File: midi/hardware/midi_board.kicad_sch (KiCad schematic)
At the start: 14 parts, among them J1 8bit_thing_bus_connector, J2 MIDI IN, J3 MIDI OUT, U1 TL16C2550PFB, U2 SLG46826G, U3 SLG46826G, U4 6N137, X1 SG-7050CCN

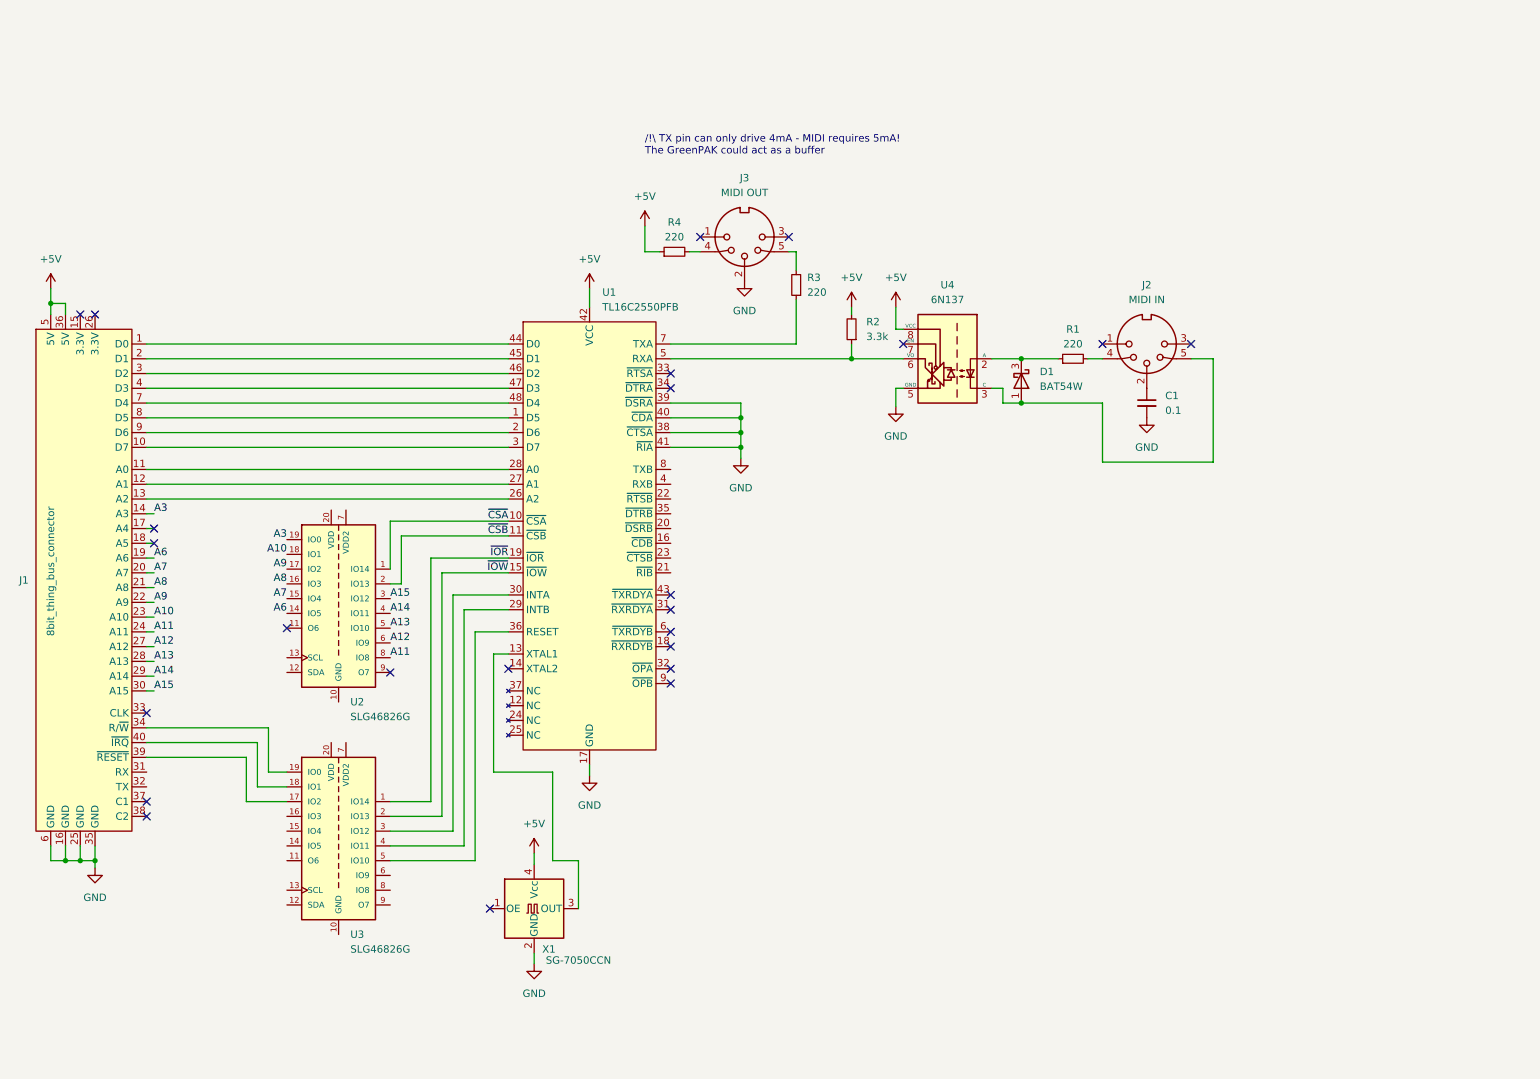
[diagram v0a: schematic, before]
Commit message: MIDI board v1 schematic & PCB
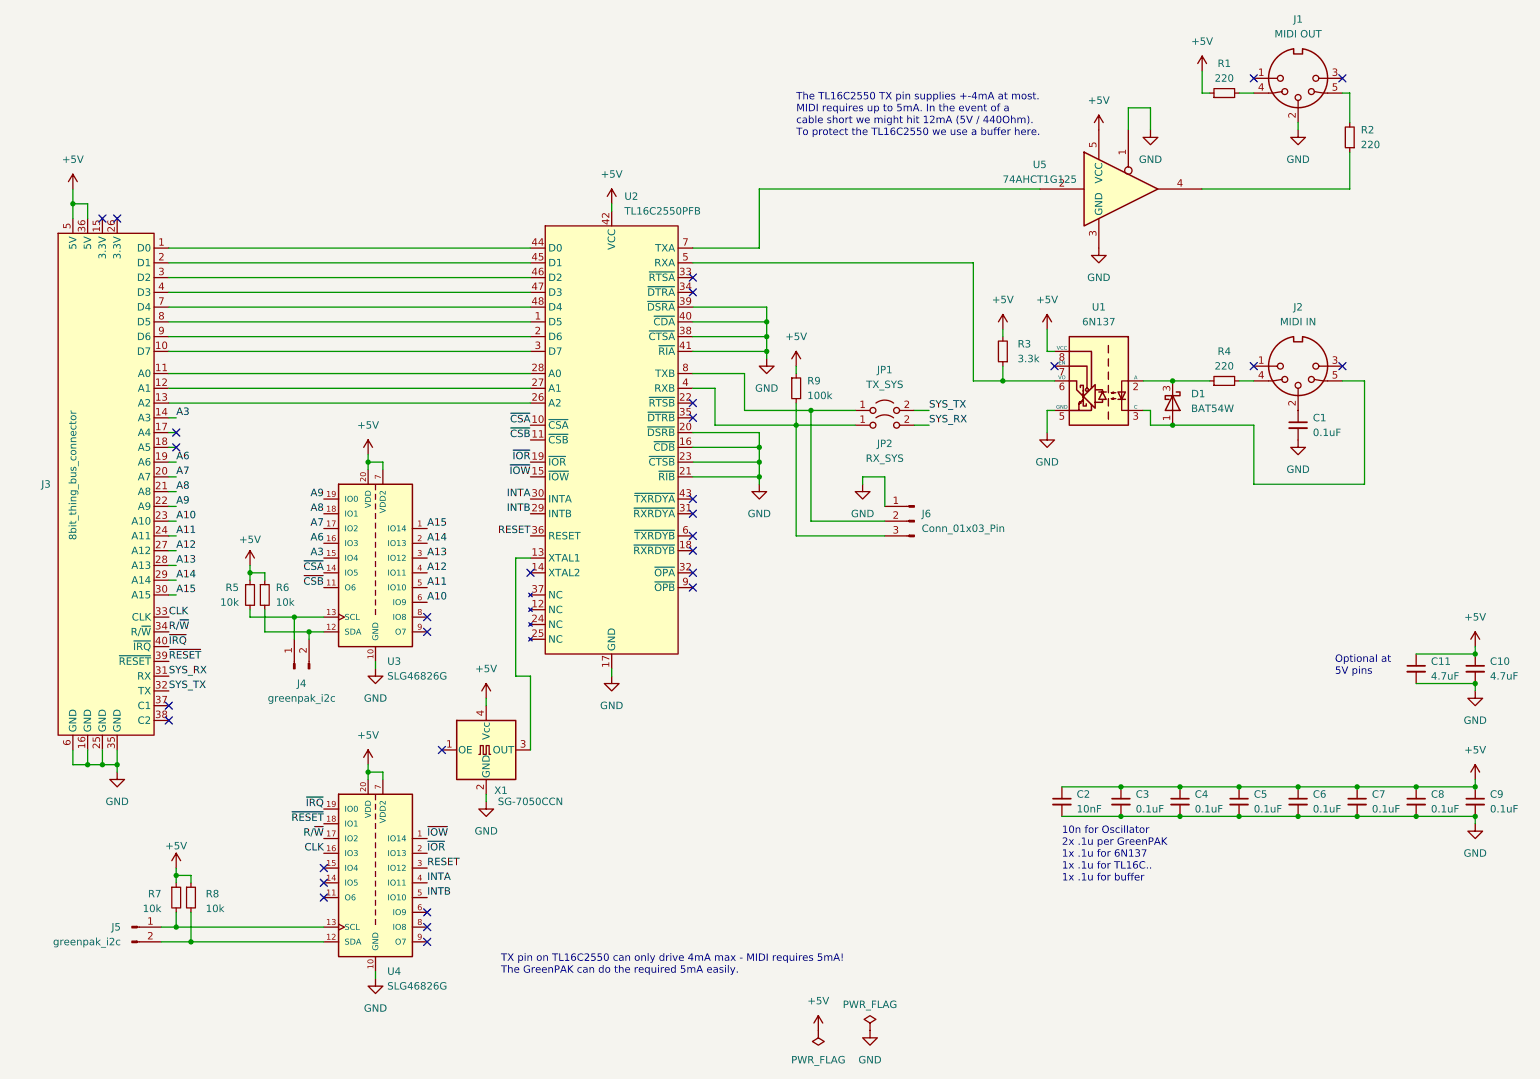
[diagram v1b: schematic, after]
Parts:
- removed J3: MIDI OUT, symbol Connector:DIN-5_180degree
- removed R3, R4: 220, symbol Device:R_Small
- added C10, C11: 4.7uF, Capacitor_SMD:C_0805_2012Metric_Pad1.18x1.45mm_HandSolder, symbol Device:C_Small
- added C2: 10nF, Capacitor_SMD:C_0805_2012Metric_Pad1.18x1.45mm_HandSolder, symbol Device:C_Small
- added C3, C4, C5, C6, C7, C8, C9: 0.1uF, Capacitor_SMD:C_0805_2012Metric_Pad1.18x1.45mm_HandSolder, symbol Device:C_Small
- added J1: MIDI OUT, own_footprints:Kycon-KCDX-5S-N, symbol Connector:DIN-5_180degree
- added J4, J5: greenpak_i2c, own_footprints:PinHeader_1x02_P2.54mm_Vertical_minimal, symbol Connector:Conn_01x02_Pin
- added J6: Conn_01x03_Pin, Connector_PinHeader_2.54mm:PinHeader_1x03_P2.54mm_Horizontal, symbol Connector:Conn_01x03_Pin
- added JP1: TX_SYS, own_footprints:PinHeader_1x02_P2.54mm_Vertical_minimal, symbol Jumper:Jumper_2_Open
- added JP2: RX_SYS, own_footprints:PinHeader_1x02_P2.54mm_Vertical_minimal, symbol Jumper:Jumper_2_Open
- added R1, R2: 220, Resistor_SMD:R_0805_2012Metric_Pad1.20x1.40mm_HandSolder, symbol Device:R_Small
- added R5, R6, R7, R8: 10k, Resistor_SMD:R_0805_2012Metric_Pad1.20x1.40mm_HandSolder, symbol Device:R_Small
- added R9: 100k, Resistor_SMD:R_0805_2012Metric_Pad1.20x1.40mm_HandSolder, symbol Device:R_Small
- added U5: 74AHCT1G125, Package_TO_SOT_SMD:SOT-353_SC-70-5_Handsoldering, symbol 74xGxx:74AHCT1G125
- C1: value 0.1 -> 0.1uF; footprint (none) -> Capacitor_SMD:C_0805_2012Metric_Pad1.18x1.45mm_HandSolder
- D1: footprint Package_TO_SOT_SMD:SOT-323_SC-70 -> Package_TO_SOT_SMD:SOT-323_SC-70_Handsoldering
- J2: footprint (none) -> own_footprints:Kycon-KCDX-5S-N
- R3: renamed from R2; footprint (none) -> Resistor_SMD:R_0805_2012Metric_Pad1.20x1.40mm_HandSolder
- R4: renamed from R1; footprint (none) -> Capacitor_SMD:C_0805_2012Metric_Pad1.18x1.45mm_HandSolder
- U3: renamed from U2; footprint SOP65P640X120-20N -> imported_footprints:SOP65P640X120-20N
- U4: renamed from U3; footprint SOP65P640X120-20N -> imported_footprints:SOP65P640X120-20N
- renumbered J1 to J3, U4 to U1, U1 to U2
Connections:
- net +5V: now also U3.20 (VDD), U3.7 (VDD2), U4.20 (VDD), U4.7 (VDD2), C10.1, C11.1, C2.1, C3.1, C4.1, C5.1, C6.1, C7.1, C8.1, C9.1, R1.1, R5.1, R6.1, R7.1, R8.1, R9.1, U5.5 (VCC)
- net A10: now also U3.6 (IO9); no longer U3.18 (IO1)
- net A11: now also U3.5 (IO10); no longer U3.8 (IO8)
- net A12: now also U3.4 (IO11); no longer U3.6 (IO9)
- net A13: now also U3.3 (IO12); no longer U3.5 (IO10)
- net A14: now also U3.2 (IO13); no longer U3.4 (IO11)
- net A15: now also U3.1 (IO14); no longer U3.3 (IO12)
- net A3: now also U3.15 (IO4); no longer U3.19 (IO0)
- net A6: now also U3.16 (IO3); no longer U3.14 (IO5)
- net A7: now also U3.17 (IO2); no longer U3.15 (IO4)
- net A8: now also U3.18 (IO1); no longer U3.16 (IO3)
- net A9: now also U3.19 (IO0); no longer U3.17 (IO2)
- net GND: now also U2.16 (~{CDB}), U2.20 (~{DSRB}), U2.21 (~{RIB}), U2.23 (~{CTSB}), U3.10 (GND), U4.10 (GND), C10.2, C11.2, C2.2, C3.2, C4.2, C5.2, C6.2, C7.2, C8.2, C9.2, J1.2, J6.1 (Pin_1), U5.1, U5.3 (GND)
- net ~{CSA}: now also U3.14 (IO5); no longer U3.1 (IO14)
- net ~{CSB}: now also U3.11 (O6); no longer U3.2 (IO13)
- net ~{IOR}: now also U4.2 (IO13); no longer U4.1 (IO14)
- net ~{IOW}: now also U4.1 (IO14); no longer U4.2 (IO13)
- net at U3.12 (SDA): now also J4.2 (Pin_2), R6.2
- net at U3.13 (SCL): now also J4.1 (Pin_1), R5.2
- net INTA: now reaches U4.4 (IO11)
- net INTA: now also U2.30 (INTA); no longer U2.29 (INTB)
- net RESET: now reaches U4.3 (IO12)
- net RESET: now also U2.36 (RESET); no longer U2.30 (INTA)
- net INTB: now reaches U4.5 (IO10)
- net INTB: now also U2.29 (INTB); no longer U2.36 (RESET)
- net at U2.4 (RXB): now also J6.3 (Pin_3), JP2.1 (A), R9.2
- net at U2.7 (TXA): now also U5.2
- net at U2.8 (TXB): now also J6.2 (Pin_2), JP1.1 (A)
- net SYS_RX: now reaches J3.31 (RX)
- net SYS_RX: now also JP2.2 (B)
- net SYS_TX: now reaches J3.32 (TX)
- net SYS_TX: now also JP1.2 (B)
- net CLK: now reaches J3.33 (CLK)
- net CLK: now also U4.16 (IO3)
- net R/~{W}: now reaches J3.34 (R/~{W})
- net R/~{W}: now also U4.17 (IO2); no longer U4.19 (IO0)
- net ~{RESET}: now reaches J3.39 (~{RESET})
- net ~{RESET}: now also U4.18 (IO1); no longer U4.17 (IO2)
- net ~{IRQ}: now reaches J3.40 (~{IRQ})
- net ~{IRQ}: now also U4.19 (IO0); no longer U4.18 (IO1)
- net at U4.12 (SDA): now also J5.2 (Pin_2), R8.2
- net at U4.13 (SCL): now also J5.1 (Pin_1), R7.2
- new net: J1.4, R1.2
- new net: J1.5, R2.2
- new net: R2.1, U5.4
- no-connect marks 24 -> 31
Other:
- note added: "10n for Oscillator 2x .1u per GreenPAK 1x .1u for 6N137 1x .1u for TL16C.. 1x .1u for buffer"
- note added: "Optional at 5V pins"
- note added: "TX pin on TL16C2550 can only drive 4mA max - MIDI requires 5mA! The GreenPAK can do the required 5mA easily."
- note added: "The TL16C2550 TX pin supplies +-4mA at most. MIDI requires up to 5mA. In the event of a cable short we might hit 12mA (5V / 440Ohm). To protect the TL16C2550 we use a buffer here."
- note removed: "/!\ TX pin can only drive 4mA - MIDI requires 5mA! The GreenPAK could act as a buffer"
- title: (none) -> 8-bit thing, MIDI board
- moved on the sheet: C1, D1, J2, J3, R3, R4, U1, U2, U3, U4, X1

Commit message: Final v1 version of the MIDI/UART board
- Tightened the layout a bit
- Added jumpers to select whether the second MIDI port is OUT or THRU
- Moved jumpers for system RX/TX connection to a better place
- Added labels for everything on the silkscreen
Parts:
- added JP3: Out/Thru select, own_footprints:PinHeader_1x03_P2.54mm_2_options_jumper_reverse, symbol Jumper:Jumper_3_Bridged12
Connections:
- net at R3.1, U1.6 (VO), U2.5 (RXA): now also JP3.1 (A)
- net at U2.7 (TXA): now also JP3.3 (B); no longer U5.2
- new net: JP3.2 (C), U5.2
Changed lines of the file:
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@@
   (junction (at 53.34 173.99) (diameter 0) (color 0 0 0 0)
+  )
+  (junction (at 172.72 57.15) (diameter 0) (color 0 0 0 0)
   )
   (junction (at 38.1 143.51) (diameter 0) (color 0 0 0 0)
@@
   (no_connect (at 93.98 171.45))
   (no_connect (at 49.53 135.89))
+  (wire (pts (xy 176.53 50.8) (xy 193.04 50.8))
+    (stroke (width 0) (type default))
+  )
   (wire (pts (xy 222.25 85.09) (xy 236.22 85.09))
     (stroke (width 0) (type default))
@@
     (stroke (width 0) (type default))
   )
+  (wire (pts (xy 193.04 44.45) (xy 199.39 44.45))
+    (stroke (width 0) (type default))
+  )
   (wire (pts (xy 63.5 110.49) (xy 66.04 110.49))
     (stroke (width 0) (type default))
@@
     (stroke (width 0) (type default))
   )
-  (wire (pts (xy 139.7 57.15) (xy 187.96 57.15))
+  (wire (pts (xy 139.7 57.15) (xy 172.72 57.15))
     (stroke (width 0) (type default))
   )
@@
     (stroke (width 0) (type default))
   )
+  (wire (pts (xy 172.72 57.15) (xy 187.96 57.15))
+    (stroke (width 0) (type default))
+  )
   (wire (pts (xy 53.34 163.83) (xy 53.34 162.56))
     (stroke (width 0) (type default))
@@
     (stroke (width 0) (type default))
   )
+  (wire (pts (xy 151.13 44.45) (xy 172.72 44.45))
+    (stroke (width 0) (type default))
+  )
   (wire (pts (xy 233.68 27.94) (xy 236.22 27.94))
     (stroke (width 0) (type default))
@@
     (stroke (width 0) (type default))
   )
-  (wire (pts (xy 151.13 44.45) (xy 199.39 44.45))
-    (stroke (width 0) (type default))
-  )
   (wire (pts (xy 35.56 140.97) (xy 35.56 143.51))
     (stroke (width 0) (type default))
@@
   )
   (wire (pts (xy 218.44 30.48) (xy 218.44 34.29))
+    (stroke (width 0) (type default))
+  )
+  (wire (pts (xy 193.04 50.8) (xy 193.04 44.45))
     (stroke (width 0) (type default))
   )
@@
         )
       )
+    )
+  )
+  (symbol (lib_id "Jumper:Jumper_3_Bridged12") (at 172.72 50.8 90) (unit 1)
+    (in_bom yes) (on_board yes) (dnp no) (fields_autoplaced)
+    (property "Reference" "JP3" (at 170.18 49.53 90)
+      (effects (font (size 1.27 1.27)) (justify left))
+    )
+    (property "Value" "Out/Thru select" (at 170.18 52.07 90)
+      (effects (font (size 1.27 1.27)) (justify left))
+    )
+    (property "Footprint" "own_footprints:PinHeader_1x03_P2.54mm_2_options_jumper_reverse" (at 172.72 50.8 0)
+      (effects (font (size 1.27 1.27)) hide)
+    )
+    (property "Datasheet" "~" (at 172.72 50.8 0)
+      (effects (font (size 1.27 1.27)) hide)
+    )
+    (pin "2")
+    (pin "1")
+    (pin "3")
+    (instances
+      (project "midi_board"
+        (path "/71530f50-7894-4efa-aa4a-2cca5f8bfb76"
+          (reference "JP3") (unit 1)
+        )
+      )

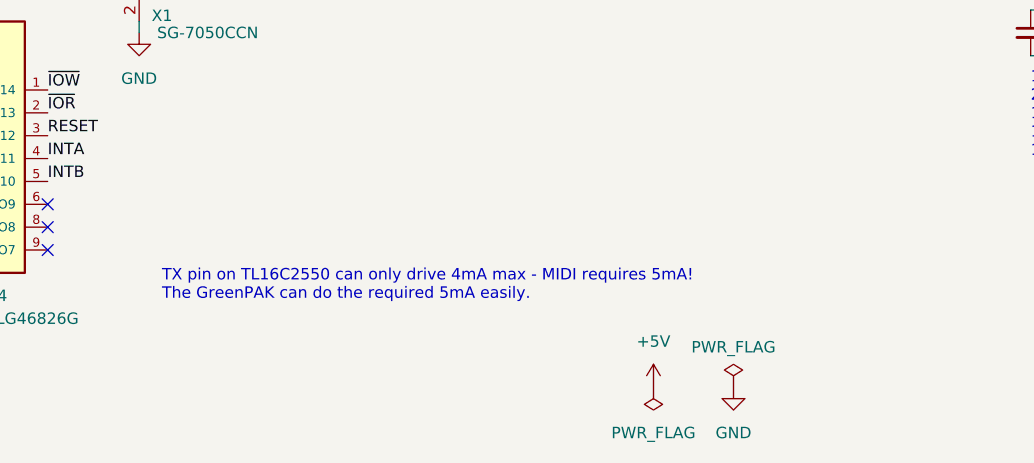
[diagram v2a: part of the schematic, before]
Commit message: MIDI board: remove outdated comment from schematic
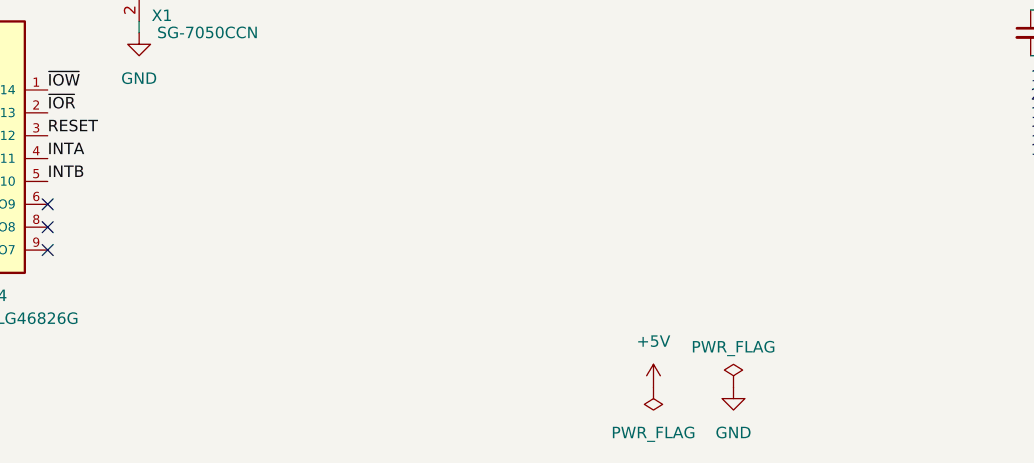
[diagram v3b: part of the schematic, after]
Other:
- note removed: "TX pin on TL16C2550 can only drive 4mA max - MIDI requires 5mA! The GreenPAK can do the required 5mA easily."
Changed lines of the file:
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@@
     (stroke (width 0) (type default))
-  )
-  (text "TX pin on TL16C2550 can only drive 4mA max - MIDI requires 5mA!\nThe GreenPAK can do the required 5mA easily."
-    (at 106.68 179.705 0)
-    (effects (font (size 1.27 1.27)) (justify left bottom))
   )
   (text "The TL16C2550 TX pin supplies +-4mA at most.\nMIDI requires up to 5mA. In the event of a\ncable short we might hit 12mA (5V / 440Ohm).\nTo protect the TL16C2550 we use a buffer here."
@@
       (effects (font (size 1.27 1.27)) hide)
     )
-    (pin "2")
-    (pin "1")
+    (pin "1")
+    (pin "2")
     (instances
       (project "midi_board"
@@
       (effects (font (size 1.27 1.27)) hide)
     )
-    (pin "2")
-    (pin "1")
+    (pin "1")
+    (pin "2")
     (instances
       (project "midi_board"
@@
       (effects (font (size 1.27 1.27)) hide)
     )
+    (pin "1")
+    (pin "2")
     (pin "3")
-    (pin "1")
-    (pin "2")
     (instances
       (project "midi_board"
@@
       (effects (font (size 1.27 1.27)) hide)
     )
-    (pin "2")
-    (pin "1")
+    (pin "1")
+    (pin "2")
     (instances
       (project "midi_board"
@@
       (effects (font (size 1.27 1.27)) hide)
     )
-    (pin "2")
-    (pin "1")
+    (pin "1")
+    (pin "2")
     (instances
       (project "midi_board"
@@
       (effects (font (size 1.27 1.27)) hide)
     )
-    (pin "2")
-    (pin "1")
+    (pin "1")
+    (pin "2")
     (instances
       (project "midi_board"
@@
       (effects (font (size 1.27 1.27)) hide)
     )
-    (pin "2")
-    (pin "1")
+    (pin "1")
+    (pin "2")
     (instances
       (project "midi_board"
@@
       (effects (font (size 1.27 1.27)) hide)
     )
-    (pin "2")
-    (pin "1")
+    (pin "1")
+    (pin "2")
     (pin "3")
     (instances
@@
       (effects (font (size 1.27 1.27)) hide)
     )
-    (pin "2")
-    (pin "1")
+    (pin "1")
+    (pin "2")
     (instances
       (project "midi_board"
@@
       (effects (font (size 1.27 1.27)) hide)
     )
-    (pin "2")
-    (pin "1")
+    (pin "1")
+    (pin "2")
     (instances
       (project "midi_board"
@@
       (effects (font (size 1.27 1.27)) hide)
     )
-    (pin "2")
-    (pin "1")
+    (pin "1")
+    (pin "2")
     (instances
       (project "midi_board"
@@
       (effects (font (size 1.27 1.27)) hide)
     )
+    (pin "1")
+    (pin "2")
+    (pin "3")
+    (pin "4")
     (pin "5")
-    (pin "4")
-    (pin "1")
-    (pin "3")
-    (pin "2")
     (instances
       (project "midi_board"
@@
       (effects (font (size 1.27 1.27)) hide)
     )
-    (pin "2")
-    (pin "1")
-    (instances
-      (project "midi_board"
+    (pin "1")
+    (pin "2")
+    (instances
+      (project "midi_board"
